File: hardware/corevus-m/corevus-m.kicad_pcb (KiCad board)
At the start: 2 copper layers, 96 x 40 mm, 75 parts, among them SW1 SPDT, SW2 SPST, T1 V_{SA}, T10 Gnd, T11 Step, T12 Diag, T13 CS, T14 En, T15 Dir, T16 Gnd, T17 Step, T18 Diag, T19 V_{SA}, T2 SClk, T20 SClk, T21 MOSI, T22 Gnd, T23 MISO, T24 3.3V, T25 CS, T26 En, T27 Dir, T28 Gnd, T29 Step, T3 MOSI, T30 Diag, T31 CS, T32 En, T33 Dir, T34 Gnd, T35 Step, T36 Diag, T4 Gnd, T5 MISO, T6 3.3V, T7 CS, T8 En, T9 Dir, U1 STM32G431CBUx, U2 TPS61040DBV, U3 AMS1117-3.3, Y1 12 MHz

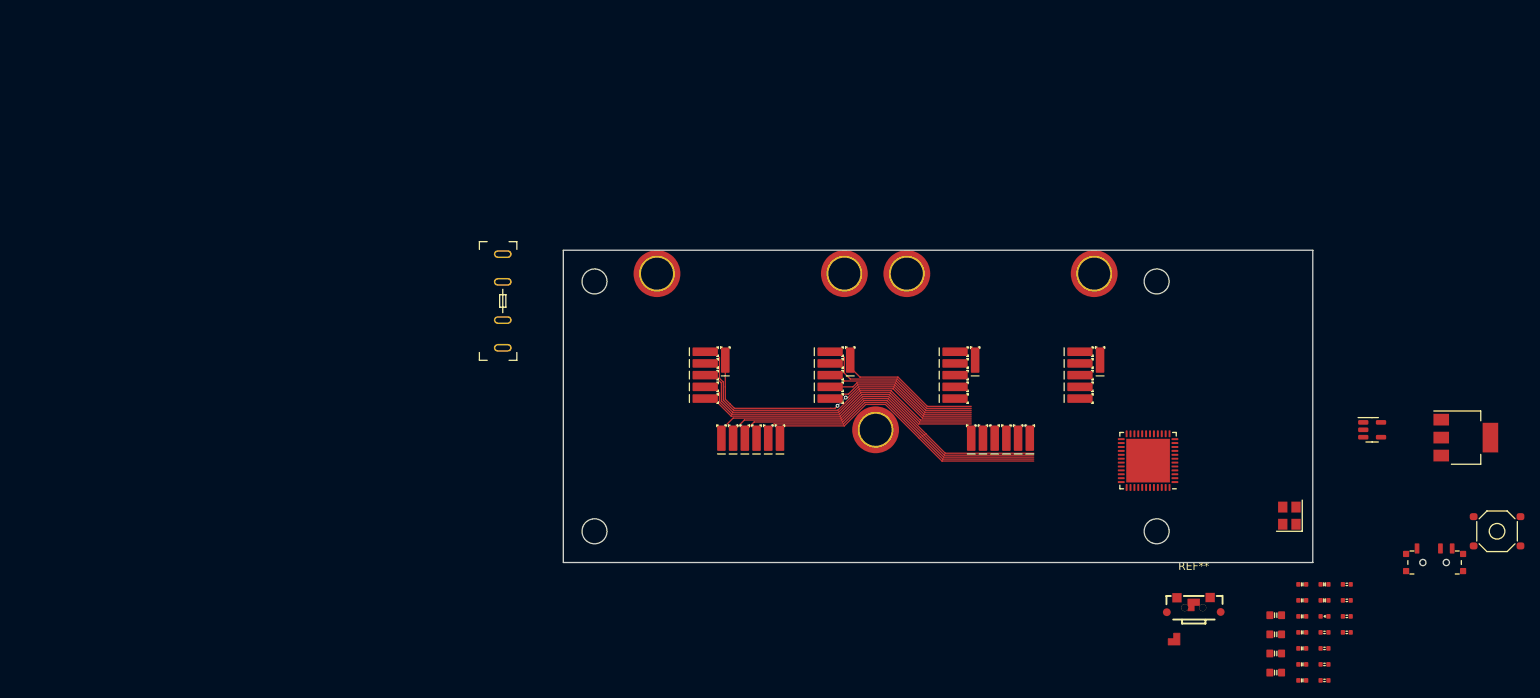
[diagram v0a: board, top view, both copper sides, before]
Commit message: finish corevus-g, create file for corevus-k
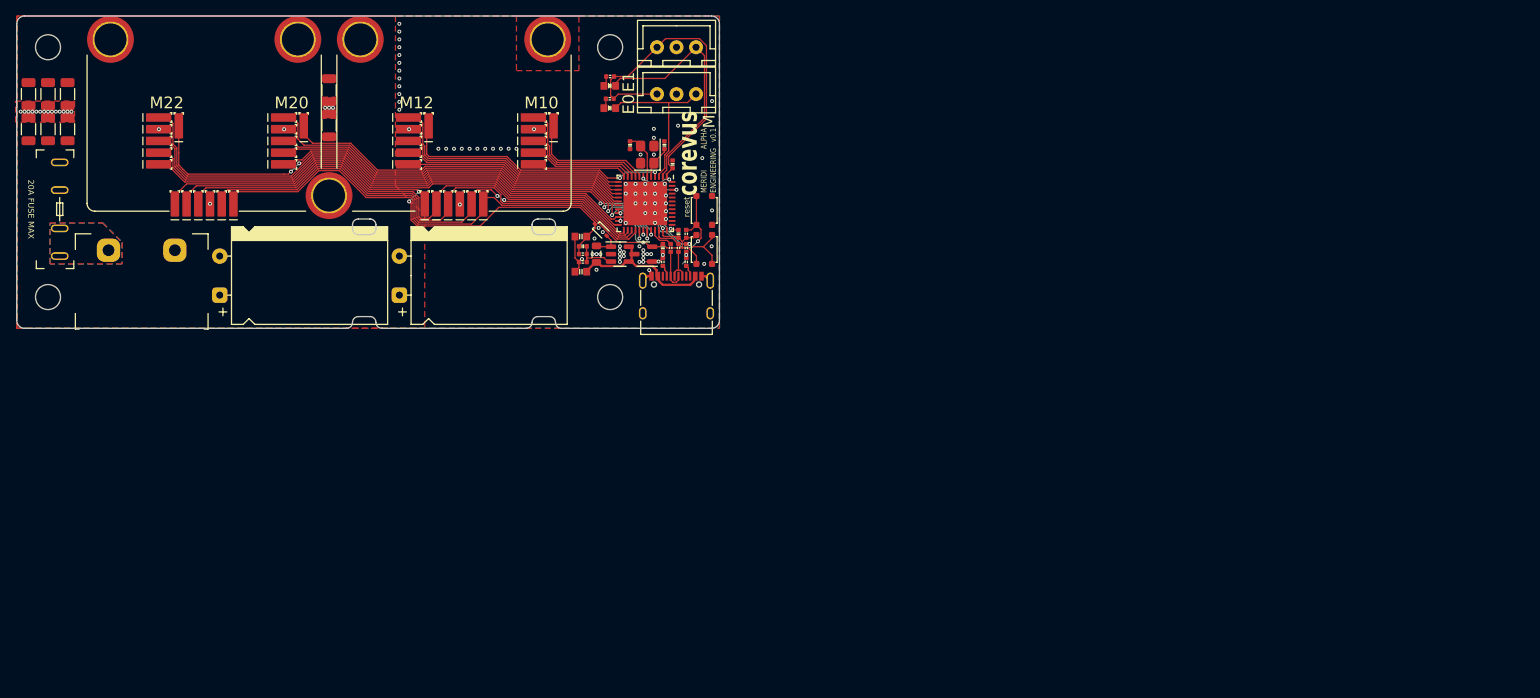
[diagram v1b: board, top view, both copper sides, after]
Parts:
- removed C10, C9: 10μF, AlphaLib:0603C
- removed C4, C5, C6: 100nF, AlphaLib:0402C
- removed R5: 330Ω, AlphaLib:0402R
- removed R6: 100kΩ, AlphaLib:0402R
- removed REF**: SW-SMD_SHOU_TS36CA-0.6, corevus:SW-SMD_SHOU_TS36CA-0.6
- added C14: 1μF 63V, Capacitor_SMD:C_1206_3216Metric, F.Cu at (51.5, 64.5)
- added C15: 1μF 63V, Capacitor_SMD:C_1206_3216Metric, F.Cu at (54.0, 64.5)
- added C16: 1μF 63V, Capacitor_SMD:C_1206_3216Metric, F.Cu at (56.5, 64.5)
- added C17: 1μF 63V, Capacitor_SMD:C_1206_3216Metric, F.Cu at (51.5, 60.0)
- added C18: 1μF 63V, Capacitor_SMD:C_1206_3216Metric, F.Cu at (54.0, 60.0)
- added C19: 1μF 63V, Capacitor_SMD:C_1206_3216Metric, F.Cu at (56.5, 60.0)
- added C20: 1μF 63V, Capacitor_SMD:C_1206_3216Metric, F.Cu at (90.0, 59.5)
- added C21: 1μF 63V, Capacitor_SMD:C_1206_3216Metric, F.Cu at (90.0, 64.0)
- added C22: 680μF 63V, corevus:CP_Radial_D12.5mm_P5.00mm_H20mm_Horizontal, F.Cu at (76.0, 83.2)
- added C23: 680μF 63V, corevus:CP_Radial_D12.5mm_P5.00mm_H20mm_Horizontal, F.Cu at (99.0, 83.2)
- added D2: Red, AlphaLib:0603LED, F.Cu at (126.0, 59.0)
- added D3: Red, AlphaLib:0603LED, F.Cu at (126.0, 61.8)
- added J1: Power In, corevus:Kefa_KF8500-8.5-2P, F.Cu at (66.0, 80.0)
- added J2: USB 2.0, corevus:USB_Type-C_16p, F.Cu at (134.5, 87.0)
- added J3: XH, corevus:JST_XH_1x03, F.Cu at (134.5, 54.0)
- added J4: XH, corevus:JST_XH_1x03, F.Cu at (134.5, 60.0)
- added L1: 10µH, Inductor_SMD:L_0805_2012Metric, F.Cu at (124.2, 80.5)
- added R10: 33Ω, AlphaLib:0402R, F.Cu at (134.8, 79.7)
- added R11: 5.1kΩ, AlphaLib:0402R, F.Cu at (132.8, 81.5)
- added R12: 5.1kΩ, AlphaLib:0402R, F.Cu at (135.8, 81.5)
- added R9: 33Ω, AlphaLib:0402R, F.Cu at (133.8, 79.7)
- C1, C2, C3: value 100nF -> 1µF
- D1: value Red -> 5819; footprint AlphaLib:0402LED -> corevus:D_SOD-323
- R2: value 1kΩ -> 200Ω
- R4: value 330Ω -> 200Ω
- SW1: value SPDT -> BOOT; footprint corevus:MSS12C02-LS -> corevus:ShouHan_TS3315A
- SW2: value SPST -> RST; footprint corevus:XKB_TS-1187A -> corevus:ShouHan_TS3315A
- U3: value AMS1117-3.3 -> XC6206P332MR; footprint Package_TO_SOT_SMD:SOT-223-3_TabPin2 -> Package_TO_SOT_SMD:SOT-23-3
- moved R4 118.0 mm to (126.0, 60.6)
- moved R2 117.2 mm to (126.0, 57.8)
- moved SW2 109.6 mm to (138.1, 74.9), turned to -90 degrees
- moved R8 109.2 mm to (122.5, 80.5)
- moved U3 107.9 mm to (130.2, 80.5), turned to 180 degrees
- moved R7 107.9 mm to (122.5, 81.5)
- moved C7 106.6 mm to (132.9, 66.5), turned to -90 degrees
- moved C12 105.3 mm to (122.5, 79.5), turned to 180 degrees
- moved C8 105.2 mm to (128.6, 66.5), turned to 90 degrees
- moved D1 105.1 mm to (124.8, 77.4), turned to -45 degrees
- moved C13 105.1 mm to (122.2, 78.2), turned to 180 degrees
- moved SW1 101.8 mm to (138.1, 79.9), turned to -90 degrees
- moved C11 101.5 mm to (122.2, 82.8), turned to 180 degrees
- moved C3 99.3 mm to (134.0, 69.0), turned to 90 degrees
- moved U2 98.9 mm to (127.2, 80.5)
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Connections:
- D1 pad 1: Net-(D1-K) -> +12V
- D1 pad 2: /BOOT0 -> Net-(D1-A)
- R1 pad 1: /BOOT0 -> GND
- R1 pad 2: GND -> /BOOT0
- R2 pad 1: GND -> Net-(D2-A)
- R2 pad 2: Net-(D1-K) -> +3.3V
- R4 pad 1: +3.3V -> Net-(D3-A)
- R4 pad 2: Net-(SW1-C) -> +3.3V
- SW1 pad 1: unconnected-(SW1-A-Pad1) -> /BOOT0
- SW1 pad 2: /BOOT0 -> +3.3V
- SW2 pad 1: Net-(R5-Pad2) -> GND
- U1 pad 10: unconnected-(U1-PA2-Pad10) -> /_{M10}Dir
- U1 pad 11: unconnected-(U1-PA3-Pad11) -> /_{M10}~{En}
- U1 pad 12: unconnected-(U1-PA4-Pad12) -> /_{M10}~{CS}
- U1 pad 13: unconnected-(U1-PA5-Pad13) -> /_{M12}Step
- U1 pad 14: unconnected-(U1-PA6-Pad14) -> /_{M12}Dir
- U1 pad 15: unconnected-(U1-PA7-Pad15) -> /_{M12}~{En}
- U1 pad 16: unconnected-(U1-PC4-Pad16) -> /_{M12}~{CS}
- U1 pad 17: unconnected-(U1-PB0-Pad17) -> /_{M20}Diag
- U1 pad 18: unconnected-(U1-PB1-Pad18) -> /_{M20}Step
- U1 pad 19: unconnected-(U1-PB2-Pad19) -> /_{M20}Dir
- U1 pad 2: unconnected-(U1-PC13-Pad2) -> /E0
- U1 pad 22: unconnected-(U1-PB10-Pad22) -> /_{M22}Dir
- U1 pad 24: unconnected-(U1-PB11-Pad24) -> /_{M22}~{En}
- U1 pad 25: unconnected-(U1-PB12-Pad25) -> /_{M22}~{CS}
- U1 pad 29: unconnected-(U1-PC6-Pad29) -> /_{M20}~{En}
- U1 pad 3: unconnected-(U1-PC14-Pad3) -> /E1
- U1 pad 30: unconnected-(U1-PA8-Pad30) -> /_{M20}~{CS}
- U1 pad 31: unconnected-(U1-PA9-Pad31) -> /_{M22}Diag
- U1 pad 32: unconnected-(U1-PA10-Pad32) -> /_{M22}Step
- U1 pad 33: unconnected-(U1-PA11-Pad33) -> Net-(U1-PA11)
- U1 pad 34: unconnected-(U1-PA12-Pad34) -> Net-(U1-PA12)
- U1 pad 4: unconnected-(U1-PC15-Pad4) -> /_{M12}Diag
- U1 pad 8: unconnected-(U1-PA0-Pad8) -> /_{M10}Diag
- U1 pad 9: unconnected-(U1-PA1-Pad9) -> /_{M10}Step
- U2 pad 1: Net-(D2-A) -> Net-(D1-A)
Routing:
- net +3.3V: track 37.1 -> 134.7 mm, vias 0 -> 5
- net /_{M12}Diag: track 0.00 -> 35.9 mm, vias 0 -> 2
- net /_{M20}~{En}: track 19.0 -> 53.4 mm, vias 0 -> 2
- net /_{M22}Diag: track 40.5 -> 74.7 mm, vias 2 -> 4
- net /_{M20}~{CS}: track 19.5 -> 52.8 mm, vias 0 -> 2
- net /_{M22}Step: track 41.9 -> 75.0 mm, vias 0 -> 2
- net /E0: track 0.00 -> 31.8 mm
- net /_{M12}Step: track 0.00 -> 31.7 mm
- net /_{M12}Dir: track 0.00 -> 29.1 mm
- net /_{M22}~{CS}: track 36.9 -> 65.4 mm
- net /_{M12}~{En}: track 0.00 -> 28.0 mm
- net /_{M12}~{CS}: track 0.00 -> 27.6 mm
- net /_{M22}~{En}: track 38.1 -> 65.2 mm
- net /_{M22}Dir: track 39.3 -> 66.3 mm
- net /MOSI: track 41.7 -> 68.6 mm
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- added copper zone on F.Cu, net +48V
- added copper zone on B.Cu, net GND
- added copper zone on F.Cu, net GND
- added copper zone on B.Cu, net Net-(J1-Pin_1)
- added copper zone on F.Cu, net Net-(J1-Pin_1)
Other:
- board size 96 x 40 mm -> 90 x 40 mm
- board text added: "20A FUSE MAX"
- board text added: "ALPHA v0.1"
- board text added: "E0"
- board text added: "E1"
- board text added: "M"
- board text added: "M10"
- board text added: "M12"
- board text added: "M20"
- board text added: "M22"
- board text added: "MERIDI ENGINEERING"
- board text added: "corevus"
- board text added: "reset"

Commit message: test
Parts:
- R7: value AkΩ -> 10kΩ
- R8: value AkΩ -> 100kΩ
- turned R10 to 90 degrees
- turned R9 to 90 degrees
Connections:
- R10 pad 1: Net-(U1-PA12) -> Net-(J2-D+-PadA6)
- R10 pad 2: Net-(J2-D+-PadA6) -> Net-(U1-PA12)
- R9 pad 1: Net-(U1-PA11) -> Net-(J2-D--PadA7)
- R9 pad 2: Net-(J2-D--PadA7) -> Net-(U1-PA11)
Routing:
- net /_{M12}Diag: track 35.9 -> 33.7 mm
- net /_{M12}~{CS}: track 27.6 -> 28.7 mm
- net /_{M10}Diag: track 17.2 -> 17.9 mm
- net /_{M20}Step: track 48.1 -> 48.8 mm
- net +3.3V: track 134.7 -> 135.5 mm
- net /MOSI: track 68.6 -> 68.0 mm
- net /SCK: track 68.6 -> 68.0 mm
- net /_{M22}Diag: track 74.7 -> 75.2 mm, vias 4 -> 2
- net GND: track 13.3 -> 13.0 mm, vias 104 -> 105
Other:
- board text added: "M0"
- board text added: "M1"
- board text added: "M2"
- board text added: "M3"
- board text removed: "M10"
- board text removed: "M12"
- board text removed: "M20"
- board text removed: "M22"
